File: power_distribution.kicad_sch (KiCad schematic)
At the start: 78 parts, among them Q1 PMOS, Q10 2PNP, Q11 2NPN, Q12 PMOS, Q13 2PNP, Q14 2PNP, Q15 2PNP, Q2 PMOS, Q3 2NPN, Q4 PMOS, Q5 PMOS, Q6 PMOS, Q7 PMOS, Q8 2NPN, Q9 PMOS, U1 PAC1954

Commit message: rename libraries from luna to cynthion
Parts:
- D1, D8: footprint luna:D_SOD-123FL -> cynthion:D_SOD-123FL
- D16, D17, D19, D20, D21, D23, D24, D25, D26, D27, D28, D29: footprint luna:DFN1006-2 -> cynthion:DFN1006-2
- Q1, Q2, Q4, Q5, Q6, Q7: footprint luna:Vishay_PowerPAK_SC70-6L_Single -> cynthion:Vishay_PowerPAK_SC70-6L_Single
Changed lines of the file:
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@@
       (effects (font (size 1.27 1.27)) (justify right))
     )
-    (property "Footprint" "luna:DFN1006-2" (id 2) (at 168.91 50.165 0)
+    (property "Footprint" "cynthion:DFN1006-2" (id 2) (at 168.91 50.165 0)
       (effects (font (size 1.27 1.27)) hide)
     )
@@
     (property "Reference" "Q7" (id 0) (at 255.27 88.3752 90))
     (property "Value" "PMOS" (id 1) (at 255.27 90.9121 90))
-    (property "Footprint" "luna:Vishay_PowerPAK_SC70-6L_Single" (id 2) (at 257.81 91.44 0)
+    (property "Footprint" "cynthion:Vishay_PowerPAK_SC70-6L_Single" (id 2) (at 257.81 91.44 0)
       (effects (font (size 1.27 1.27)) hide)
     )
@@
       (effects (font (size 1.27 1.27)) (justify left))
     )
-    (property "Footprint" "luna:D_SOD-123FL" (id 2) (at 32.385 92.71 0)
+    (property "Footprint" "cynthion:D_SOD-123FL" (id 2) (at 32.385 92.71 0)
       (effects (font (size 1.27 1.27)) hide)
     )
@@
       (effects (font (size 1.27 1.27)) (justify right))
     )
-    (property "Footprint" "luna:DFN1006-2" (id 2) (at 259.715 50.165 0)
+    (property "Footprint" "cynthion:DFN1006-2" (id 2) (at 259.715 50.165 0)
       (effects (font (size 1.27 1.27)) hide)
     )
@@
       (effects (font (size 1.27 1.27)) (justify left))
     )
-    (property "Footprint" "luna:DFN1006-2" (id 2) (at 139.065 99.06 0)
+    (property "Footprint" "cynthion:DFN1006-2" (id 2) (at 139.065 99.06 0)
       (effects (font (size 1.27 1.27)) hide)
     )
@@
     (property "Reference" "Q5" (id 0) (at 197.485 88.3752 90))
     (property "Value" "PMOS" (id 1) (at 197.485 90.9121 90))
-    (property "Footprint" "luna:Vishay_PowerPAK_SC70-6L_Single" (id 2) (at 200.025 91.44 0)
+    (property "Footprint" "cynthion:Vishay_PowerPAK_SC70-6L_Single" (id 2) (at 200.025 91.44 0)
       (effects (font (size 1.27 1.27)) hide)
     )
@@
       (effects (font (size 1.27 1.27)) (justify right))
     )
-    (property "Footprint" "luna:DFN1006-2" (id 2) (at 167.64 99.06 0)
+    (property "Footprint" "cynthion:DFN1006-2" (id 2) (at 167.64 99.06 0)
       (effects (font (size 1.27 1.27)) hide)
     )
@@
       (effects (font (size 1.27 1.27)) (justify left))
     )
-    (property "Footprint" "luna:DFN1006-2" (id 2) (at 98.425 57.785 0)
+    (property "Footprint" "cynthion:DFN1006-2" (id 2) (at 98.425 57.785 0)
       (effects (font (size 1.27 1.27)) hide)
     )
@@
       (effects (font (size 1.27 1.27)) (justify left))
     )
-    (property "Footprint" "luna:DFN1006-2" (id 2) (at 140.335 50.165 0)
+    (property "Footprint" "cynthion:DFN1006-2" (id 2) (at 140.335 50.165 0)
       (effects (font (size 1.27 1.27)) hide)
     )
@@
       (effects (font (size 1.27 1.27)) (justify right))
     )
-    (property "Footprint" "luna:DFN1006-2" (id 2) (at 274.32 99.06 0)
+    (property "Footprint" "cynthion:DFN1006-2" (id 2) (at 274.32 99.06 0)
       (effects (font (size 1.27 1.27)) hide)
     )
@@
       (effects (font (size 1.27 1.27)) (justify left))
     )
-    (property "Footprint" "luna:DFN1006-2" (id 2) (at 98.425 113.03 0)
+    (property "Footprint" "cynthion:DFN1006-2" (id 2) (at 98.425 113.03 0)
       (effects (font (size 1.27 1.27)) hide)
     )
@@
       (effects (font (size 1.27 1.27)) (justify right))
     )
-    (property "Footprint" "luna:DFN1006-2" (id 2) (at 23.495 97.79 0)
+    (property "Footprint" "cynthion:DFN1006-2" (id 2) (at 23.495 97.79 0)
       (effects (font (size 1.27 1.27)) hide)
     )
@@
       (effects (font (size 1.27 1.27)) (justify right))
     )
-    (property "Footprint" "luna:DFN1006-2" (id 2) (at 246.38 99.06 0)
+    (property "Footprint" "cynthion:DFN1006-2" (id 2) (at 246.38 99.06 0)
       (effects (font (size 1.27 1.27)) hide)
     )
@@
     (property "Reference" "Q1" (id 0) (at 159.385 39.4802 90))
     (property "Value" "PMOS" (id 1) (at 159.385 42.0171 90))
-    (property "Footprint" "luna:Vishay_PowerPAK_SC70-6L_Single" (id 2) (at 156.845 42.545 0)
+    (property "Footprint" "cynthion:Vishay_PowerPAK_SC70-6L_Single" (id 2) (at 156.845 42.545 0)
       (effects (font (size 1.27 1.27)) hide)
     )
@@
       (effects (font (size 1.27 1.27)) (justify left))
     )
-    (property "Footprint" "luna:DFN1006-2" (id 2) (at 53.975 97.79 0)
+    (property "Footprint" "cynthion:DFN1006-2" (id 2) (at 53.975 97.79 0)
       (effects (font (size 1.27 1.27)) hide)
     )
@@
     (property "Reference" "Q4" (id 0) (at 158.115 88.3752 90))
     (property "Value" "PMOS" (id 1) (at 158.115 90.9121 90))
-    (property "Footprint" "luna:Vishay_PowerPAK_SC70-6L_Single" (id 2) (at 155.575 91.44 0)
+    (property "Footprint" "cynthion:Vishay_PowerPAK_SC70-6L_Single" (id 2) (at 155.575 91.44 0)
       (effects (font (size 1.27 1.27)) hide)
     )
@@
       (effects (font (size 1.27 1.27)) (justify left))
     )
-    (property "Footprint" "luna:D_SOD-123FL" (id 2) (at 32.385 37.465 0)
+    (property "Footprint" "cynthion:D_SOD-123FL" (id 2) (at 32.385 37.465 0)
       (effects (font (size 1.27 1.27)) hide)
     )
@@
     (property "Reference" "Q6" (id 0) (at 222.885 88.3752 90))
     (property "Value" "PMOS" (id 1) (at 222.885 90.9121 90))
-    (property "Footprint" "luna:Vishay_PowerPAK_SC70-6L_Single" (id 2) (at 220.345 91.44 0)
+    (property "Footprint" "cynthion:Vishay_PowerPAK_SC70-6L_Single" (id 2) (at 220.345 91.44 0)
       (effects (font (size 1.27 1.27)) hide)
     )
@@
     (property "Reference" "Q2" (id 0) (at 198.755 39.4802 90))
     (property "Value" "PMOS" (id 1) (at 198.755 42.0171 90))
-    (property "Footprint" "luna:Vishay_PowerPAK_SC70-6L_Single" (id 2) (at 201.295 42.545 0)
+    (property "Footprint" "cynthion:Vishay_PowerPAK_SC70-6L_Single" (id 2) (at 201.295 42.545 0)
       (effects (font (size 1.27 1.27)) hide)
     )
@@
       (effects (font (size 1.27 1.27)) (justify left))
     )
-    (property "Footprint" "luna:DFN1006-2" (id 2) (at 53.975 42.545 0)
-      (effects (font (size 1.27 1.27)) hide)
-    )
+    (property "Footprint" "cynthion:DFN1006-2" (id 2) (at 53.975 42.545 0)
+      (effects (font (size 1.27 1.27)) hide)
+    )

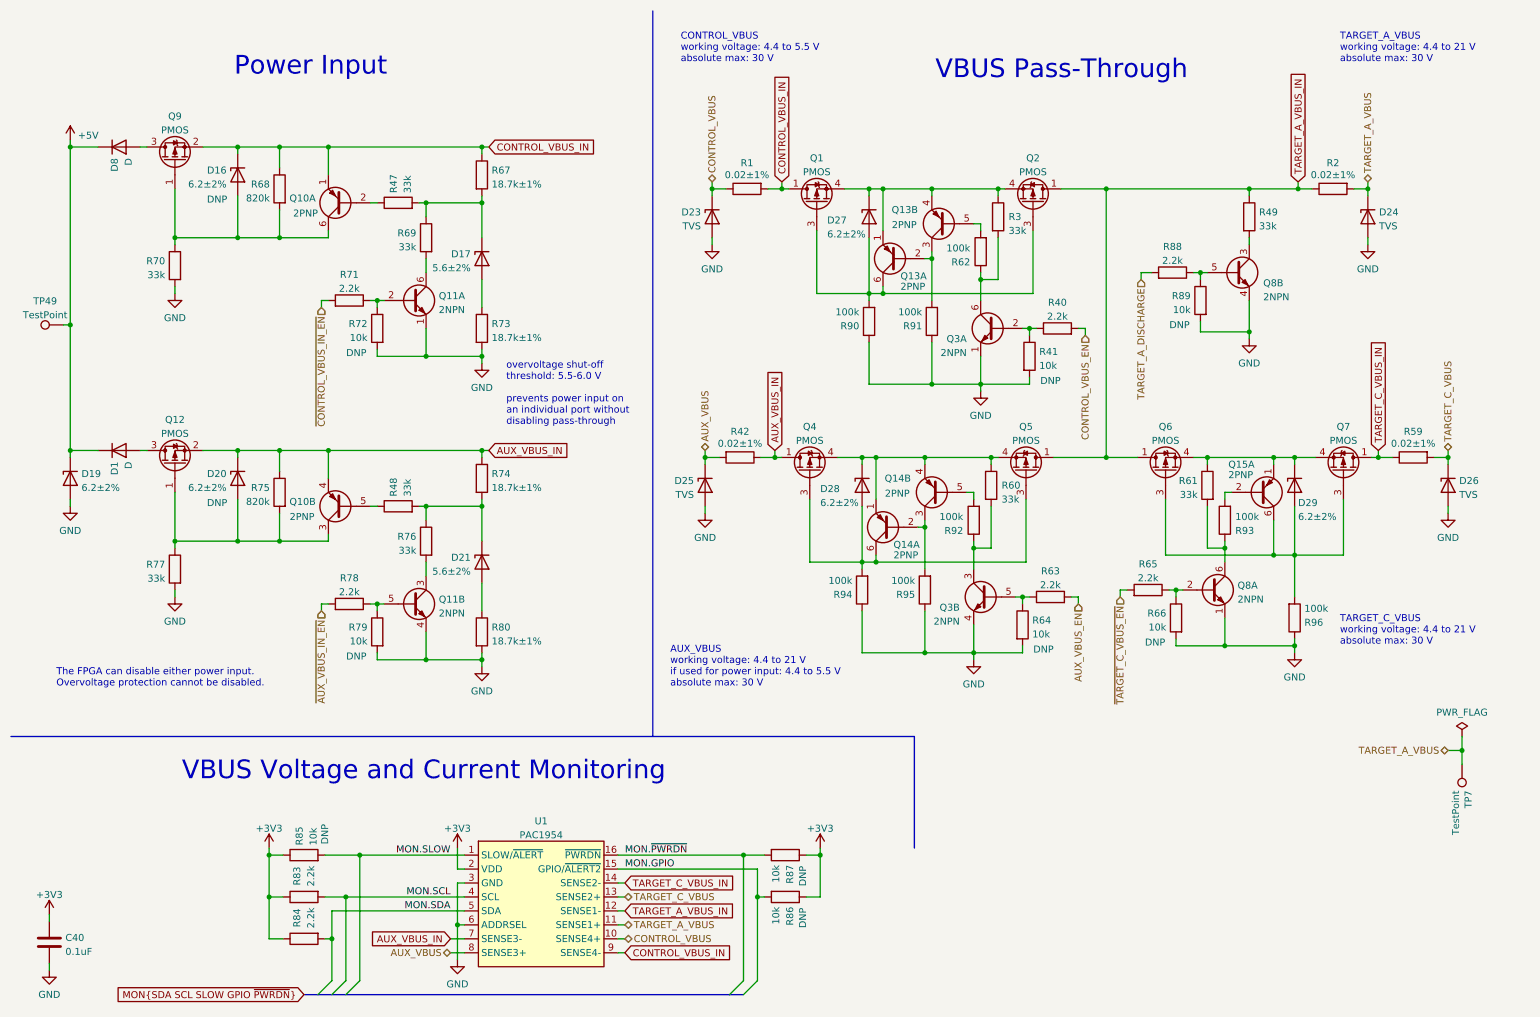
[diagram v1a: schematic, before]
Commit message: Add POWER_GOOD signal
This open collector signal is driven low to indicate that +3V3 is at a
voltage high enough for the FPGA to operate normally. It is used to gate
power input and power passthrough control outputs from the FPGA.

Fixes #9
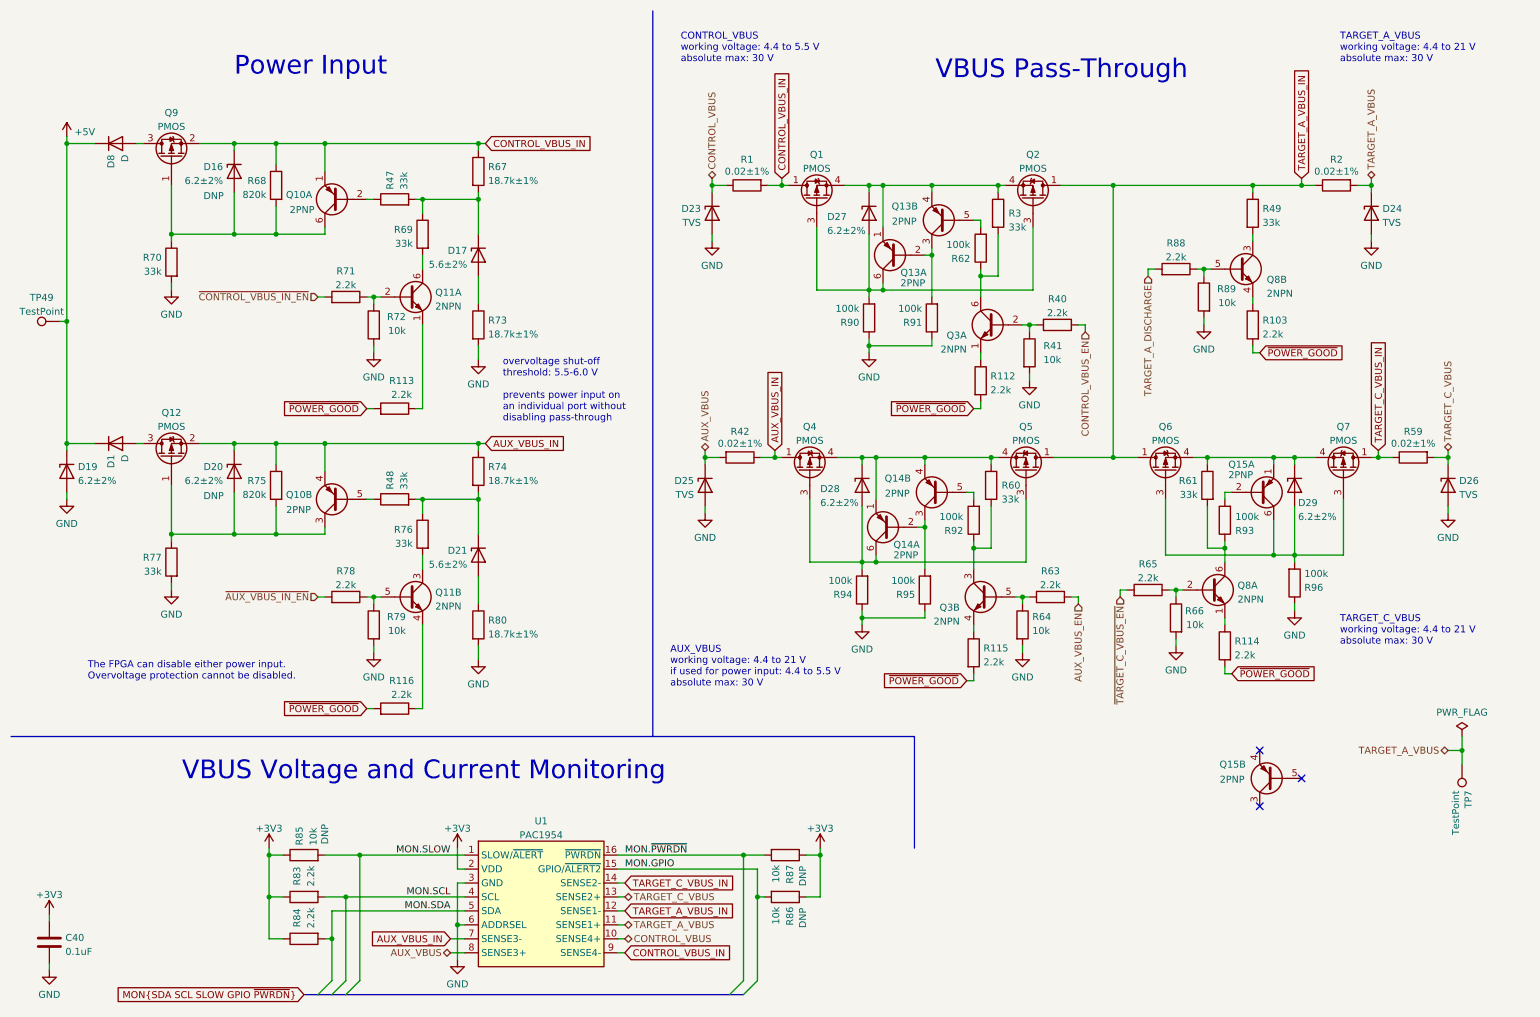
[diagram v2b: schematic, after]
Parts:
- added unit 2 of Q15
- added R103, R112, R113, R114, R115, R116: 2.2k, Resistor_SMD:R_0402_1005Metric, symbol Device:R
- R41, R64, R66, R72, R79, R89: DNP DNP -> (none)
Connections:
- net GND: no longer Q11.1 (E1), Q11.4 (E2), Q3.1 (E1), Q3.4 (E2), Q8.1 (E1), Q8.4 (E2)
- new net: Q3.1 (E1), R112.1
- new net: Q11.1 (E1), R113.1
- new net: Q8.1 (E1), R114.1
- new net: Q8.4 (E2), R103.1
- new net: Q11.4 (E2), R116.1
- new net: Q3.4 (E2), R115.1
- new net ~{POWER_GOOD}: R103.2, R112.2, R113.2, R114.2, R115.2, R116.2
- no-connect marks 0 -> 3
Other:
- moved on the sheet: D1, D16, D17, D19, D20, D21, D23, D24, D27, D8, Q1, Q10A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

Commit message: Rearrange schematic for readability
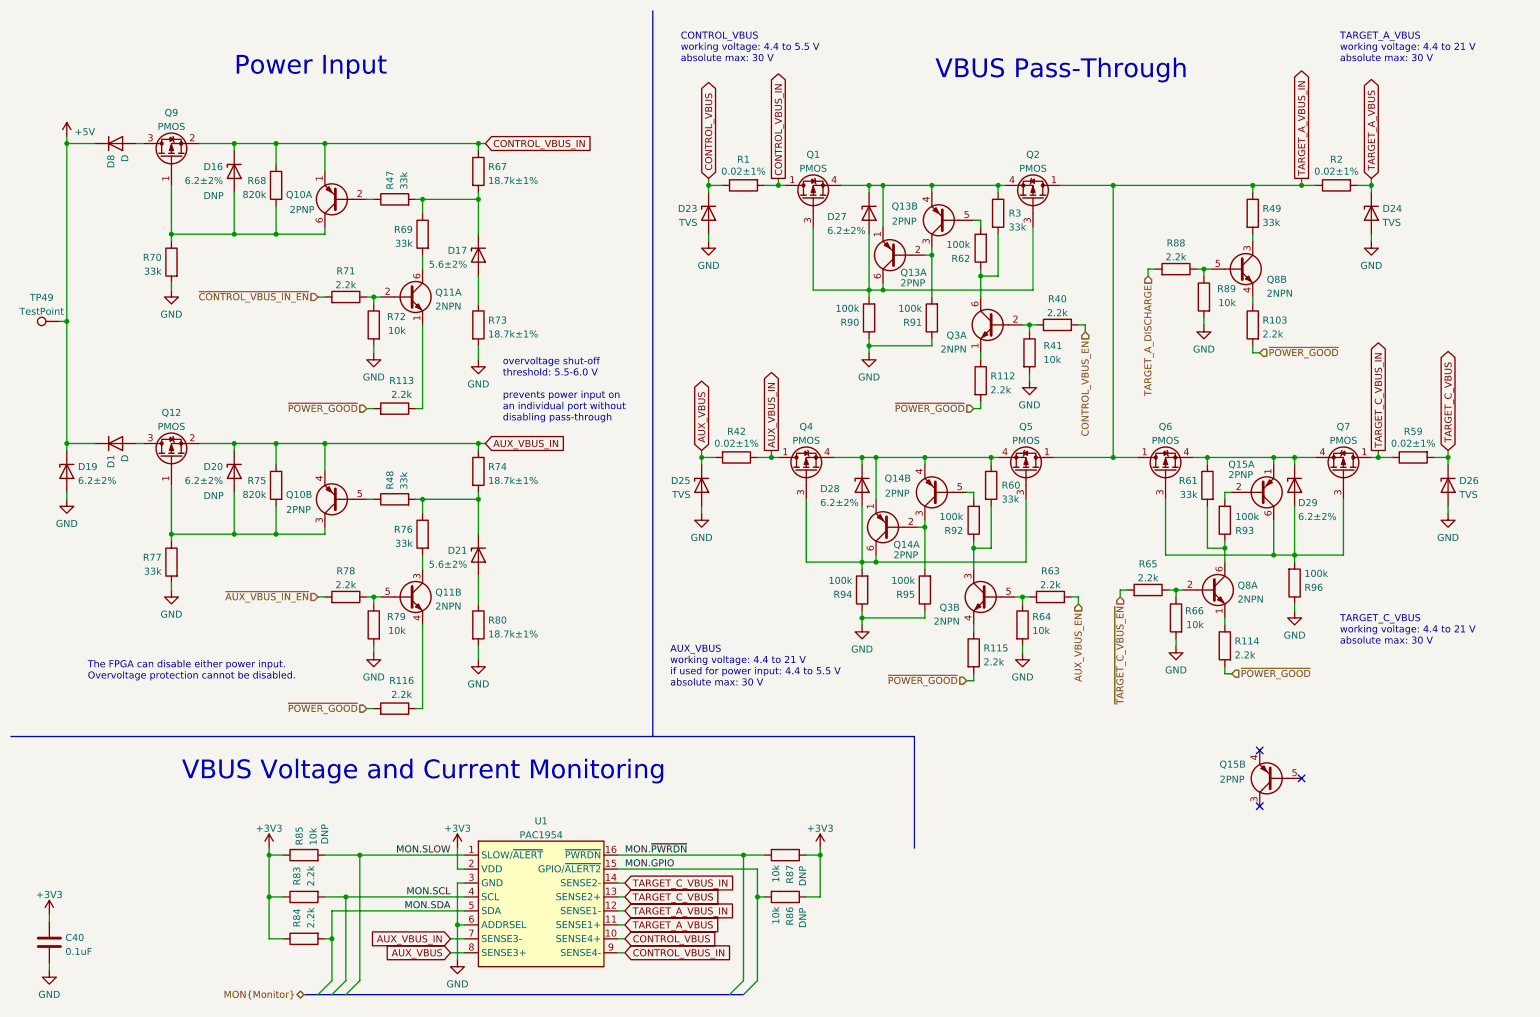
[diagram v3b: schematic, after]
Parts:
- removed TP7: TestPoint, TestPoint:TestPoint_Pad_D1.0mm, symbol Connector:TestPoint
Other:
- moved on the sheet: D23, D25, Q1, Q4, R1, R42

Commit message: Upgrade to KiCad 7
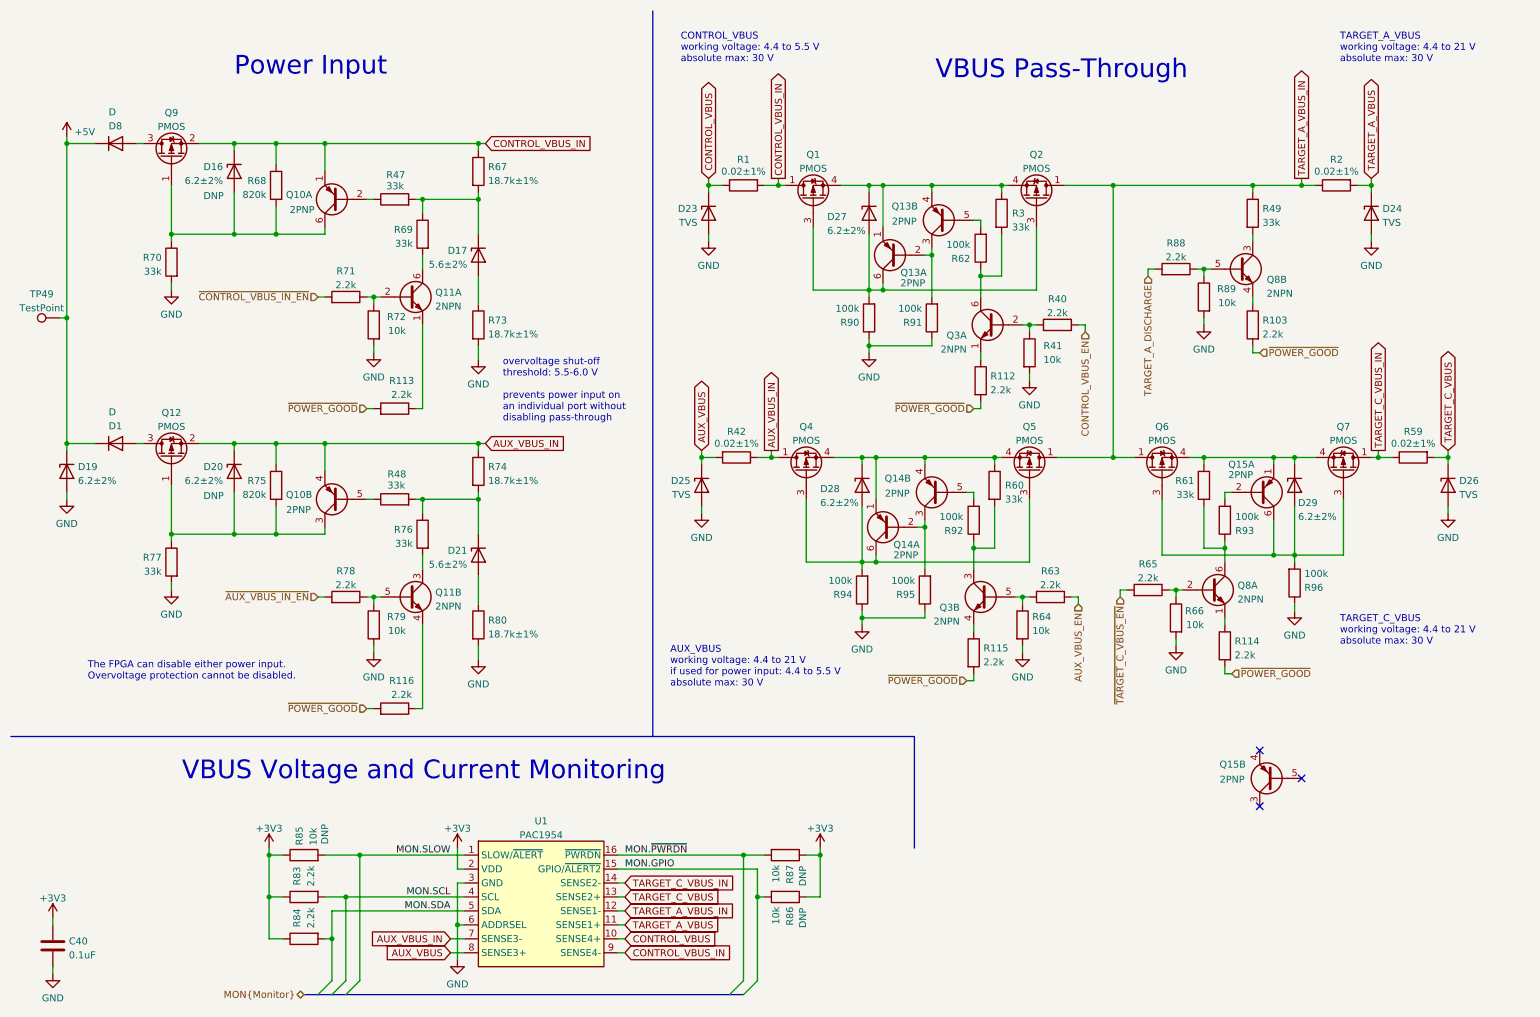
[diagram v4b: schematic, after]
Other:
- moved on the sheet: C40, Q2, Q5, Q6, R3, R60, R61, TP49
